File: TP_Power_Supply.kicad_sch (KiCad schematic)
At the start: 3 parts, among them U2 MCP1703T-3302E

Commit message: Issue 5 applied
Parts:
- U2: Developer (none) -> MW; LCSC Part #(optional) (none) -> C39051; Manufacturer (none) -> MICROCHIP TECHNOLOGY; Manufacturer Part Number (none) -> MCP1703T-3302E/CB; Package (none) -> SOT-23(SOT-23-3); Price@1000pcs (none) -> 1,49; Price@1pc (none) -> 2,04; Supplier (none) -> TME; Supplier Part Number (none) -> MCP1703T3302ECB; URL (none) -> https://www.tme.eu/pl/details/mcp1703t3302ecb/stabilizatory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
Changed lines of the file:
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@@
     (pin "2")
   )
-  (symbol (lib_id "Linear_Regulators:MCP1703T-3302E") (at 212.09 142.24 0) (unit 1)
+  (symbol (lib_name "Linear_Regulators:MCP1703T-3302E_1") (lib_id "Linear_Regulators:MCP1703T-3302E") (at 212.09 142.24 0) (unit 1)
     (in_bom yes) (on_board yes)
-    (property "Reference" "U2" (id 0) (at 212.09 132.4102 0)
+    (property "Reference" "U2" (id 0) (at 212.09 132.463 0)
       (effects (font (size 1.524 1.524)))
     )
-    (property "Value" "MCP1703T-3302E" (id 1) (at 212.09 135.1026 0)
+    (property "Value" "MCP1703T-3302E" (id 1) (at 212.09 135.1711 0)
       (effects (font (size 1.524 1.524)))
     )
@@
       (effects (font (size 1.524 1.524)) hide)
     )
-    (property "Datasheet" "Dc_Dc_Regulators/Linear/Components_Documentation/Mcp1703T_22049a.pdf" (id 3) (at 212.09 135.1026 0)
+    (property "Datasheet" "https://datasheet.lcsc.com/szlcsc/1808291012_Microchip-Tech-MCP1700T-3302E-TT_C39051.pdf" (id 3) (at 212.09 143.51 0)
       (effects (font (size 1.524 1.524)) hide)
     )
+    (property "Manufacturer" "MICROCHIP TECHNOLOGY" (id 4) (at 212.09 142.24 0)
+      (effects (font (size 1.27 1.27)) hide)
+    )
+    (property "Manufacturer Part Number" "MCP1703T-3302E/CB" (id 5) (at 212.09 142.24 0)
+      (effects (font (size 1.27 1.27)) hide)
+    )
+    (property "Supplier" "TME" (id 6) (at 212.09 142.24 0)
+      (effects (font (size 1.27 1.27)) hide)
+    )
+    (property "Supplier Part Number" "MCP1703T3302ECB" (id 7) (at 212.09 142.24 0)
+      (effects (font (size 1.27 1.27)) hide)
+    )
+    (property "URL" "https://www.tme.eu/pl/details/mcp1703t3302ecb/stabilizatory-napiecia-nieregulowane-ldo/microchip-technology/mcp1703t-3302e-cb/" (id 8) (at 212.09 142.24 0)
+      (effects (font (size 1.27 1.27)) hide)
+    )
+    (property "Price@1pc" "2,04" (id 9) (at 212.09 142.24 0)
+      (effects (font (size 1.27 1.27)) hide)
+    )
+    (property "Price@1000pcs" "1,49" (id 10) (at 212.09 142.24 0)
+      (effects (font (size 1.27 1.27)) hide)
+    )
+    (property "Developer" "MW" (id 11) (at 212.09 142.24 0)
+      (effects (font (size 1.27 1.27)) hide)
+    )
+    (property "Package" "SOT-23(SOT-23-3)" (id 12) (at 212.09 142.24 0)
+      (effects (font (size 1.27 1.27)) hide)
+    )
+    (property "LCSC Part #(optional)" "C39051" (id 13) (at 212.09 142.24 0)
+      (effects (font (size 1.27 1.27)) hide)
+    )
     (pin "1")

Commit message: Applied issue 4
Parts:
- removed C3, C4: 100nF/50V, Capacitors_Smd_0603:100nF_0603, symbol Capacitors_Smd0603:100nF_0603
- added C3, C4: 1uF/16V, Capacitors_Smd_0603:1uF_0603, symbol Capacitors_Smd0603:1uF
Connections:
- net GND: now also C3.2, C4.2
- net VIN: now also C3.1
- net VOUT_3.3V_250mA: now also C4.1
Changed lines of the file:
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@@
     (pin "1")
   )
-  (symbol (lib_id "Capacitors_Smd0603:100nF_0603") (at 191.77 147.32 0) (unit 1)
+  (symbol (lib_id "Capacitors_Smd0603:1uF") (at 191.77 147.32 0) (unit 1)
     (in_bom yes) (on_board yes)
-    (property "Reference" "C3" (id 0) (at 195.0974 146.1516 0)
+    (property "Reference" "C3" (id 0) (at 195.0975 146.1706 0)
       (effects (font (size 1.27 1.27)) (justify left))
     )
-    (property "Value" "100nF/50V" (id 1) (at 195.0974 148.463 0)
+    (property "Value" "1uF/16V" (id 1) (at 195.098 148.469 0)
       (effects (font (size 1.27 1.27)) (justify left))
     )
-    (property "Footprint" "Capacitors_Smd_0603:100nF_0603" (id 2) (at 191.77 147.32 0)
+    (property "Footprint" "Capacitors_Smd_0603:1uF_0603" (id 2) (at 187.96 142.24 0)
       (effects (font (size 1.524 1.524)) hide)
     )
-    (property "Datasheet" "Capacitors/Smd_0603/Components_Documentation/KEM_C1005_Y5V_SMD.pdf" (id 3) (at 191.77 147.32 0)
+    (property "Datasheet" "Capacitors/Smd_0603/Components_Documentation/KEM_C1005_Y5V_SMD.pdf" (id 3) (at 187.96 142.24 0)
       (effects (font (size 1.524 1.524)) hide)
     )
@@
       (effects (font (size 1.27 1.27)) hide)
     )
-    (property "Manufacturer Part Number" "CL10B104JB8NNNC" (id 5) (at 191.77 147.32 0)
+    (property "Manufacturer Part Number" "CL10B105KO8NNNC" (id 5) (at 191.77 147.32 0)
       (effects (font (size 1.27 1.27)) hide)
     )
@@
       (effects (font (size 1.27 1.27)) hide)
     )
-    (property "Supplier Part Number" "CL10B104JB8NNNC" (id 7) (at 191.77 147.32 0)
+    (property "Supplier Part Number" "CL10B105KO8NNNC" (id 7) (at 191.77 147.32 0)
       (effects (font (size 1.27 1.27)) hide)
     )
-    (property "URL" "https://www.tme.eu/pl/details/cl10b104jb8nnnc/kondensatory-mlcc-smd-0603/samsung/" (id 8) (at 191.77 147.32 0)
+    (property "URL" "https://www.tme.eu/pl/details/cl10b105ko8nnnc/kondensatory-mlcc-smd-0603/samsung/" (id 8) (at 191.77 147.32 0)
       (effects (font (size 1.27 1.27)) hide)
     )
-    (property "Price@1pc" "0,04540" (id 9) (at 191.77 147.32 0)
+    (property "Price@1pc" "0,07530" (id 9) (at 191.77 147.32 0)
       (effects (font (size 1.27 1.27)) hide)
     )
-    (property "Price@1000pcs" "0,02231" (id 10) (at 191.77 147.32 0)
+    (property "Price@1000pcs" "0,03514" (id 10) (at 191.77 147.32 0)
       (effects (font (size 1.27 1.27)) hide)
     )
@@
     (pin "2")
   )
-  (symbol (lib_id "Capacitors_Smd0603:100nF_0603") (at 232.41 147.32 0) (unit 1)
+  (symbol (lib_id "Capacitors_Smd0603:1uF") (at 232.41 147.32 0) (unit 1)
     (in_bom yes) (on_board yes)
-    (property "Reference" "C4" (id 0) (at 235.7374 146.1516 0)
+    (property "Reference" "C4" (id 0) (at 235.7375 146.1706 0)
       (effects (font (size 1.27 1.27)) (justify left))
     )
-    (property "Value" "100nF/50V" (id 1) (at 235.7374 148.463 0)
+    (property "Value" "1uF/16V" (id 1) (at 235.738 148.469 0)
       (effects (font (size 1.27 1.27)) (justify left))
     )
-    (property "Footprint" "Capacitors_Smd_0603:100nF_0603" (id 2) (at 232.41 147.32 0)
+    (property "Footprint" "Capacitors_Smd_0603:1uF_0603" (id 2) (at 228.6 142.24 0)
       (effects (font (size 1.524 1.524)) hide)
     )
-    (property "Datasheet" "Capacitors/Smd_0603/Components_Documentation/KEM_C1005_Y5V_SMD.pdf" (id 3) (at 232.41 147.32 0)
+    (property "Datasheet" "Capacitors/Smd_0603/Components_Documentation/KEM_C1005_Y5V_SMD.pdf" (id 3) (at 228.6 142.24 0)
       (effects (font (size 1.524 1.524)) hide)
     )
@@
       (effects (font (size 1.27 1.27)) hide)
     )
-    (property "Manufacturer Part Number" "CL10B104JB8NNNC" (id 5) (at 232.41 147.32 0)
+    (property "Manufacturer Part Number" "CL10B105KO8NNNC" (id 5) (at 232.41 147.32 0)
       (effects (font (size 1.27 1.27)) hide)
     )
@@
       (effects (font (size 1.27 1.27)) hide)
     )
-    (property "Supplier Part Number" "CL10B104JB8NNNC" (id 7) (at 232.41 147.32 0)
+    (property "Supplier Part Number" "CL10B105KO8NNNC" (id 7) (at 232.41 147.32 0)
       (effects (font (size 1.27 1.27)) hide)
     )
-    (property "URL" "https://www.tme.eu/pl/details/cl10b104jb8nnnc/kondensatory-mlcc-smd-0603/samsung/" (id 8) (at 232.41 147.32 0)
+    (property "URL" "https://www.tme.eu/pl/details/cl10b105ko8nnnc/kondensatory-mlcc-smd-0603/samsung/" (id 8) (at 232.41 147.32 0)
       (effects (font (size 1.27 1.27)) hide)
     )
-    (property "Price@1pc" "0,04540" (id 9) (at 232.41 147.32 0)
+    (property "Price@1pc" "0,07530" (id 9) (at 232.41 147.32 0)
       (effects (font (size 1.27 1.27)) hide)
     )
-    (property "Price@1000pcs" "0,02231" (id 10) (at 232.41 147.32 0)
+    (property "Price@1000pcs" "0,03514" (id 10) (at 232.41 147.32 0)
       (effects (font (size 1.27 1.27)) hide)
     )

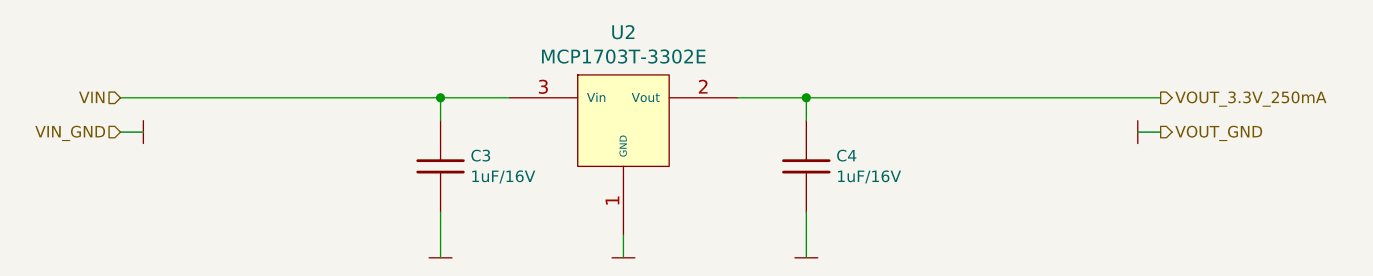
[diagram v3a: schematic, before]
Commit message: Reworked schematic and applied changes on pcb related with mini pci express
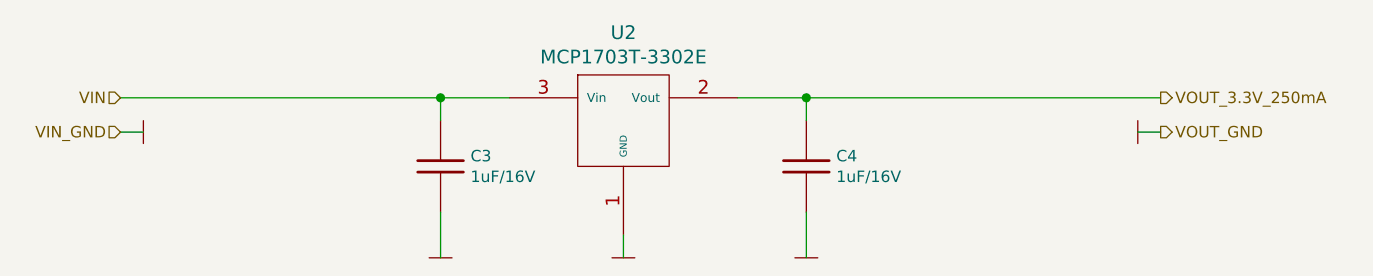
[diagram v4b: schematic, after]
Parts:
- removed C3, C4: 1uF/16V, Capacitors_Smd_0603:1uF_0603, symbol Capacitors_Smd0603:1uF
- added C3, C4: 1uF/16V, Capacitors_Smd_0603:1uF_0603, symbol Capacitors_Smd0603:1uF_0603
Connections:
- net GND: now also C3.2, C4.2
- net VIN: now also C3.1
- net VOUT_3.3V_250mA: now also C4.1
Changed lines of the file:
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@@
     (pin "1")
   )
-  (symbol (lib_id "Capacitors_Smd0603:1uF") (at 191.77 147.32 0) (unit 1)
+  (symbol (lib_id "Capacitors_Smd0603:1uF_0603") (at 191.77 147.32 0) (unit 1)
     (in_bom yes) (on_board yes)
-    (property "Reference" "C3" (id 0) (at 195.0975 146.1706 0)
+    (property "Reference" "C3" (id 0) (at 195.098 146.171 0)
       (effects (font (size 1.27 1.27)) (justify left))
     )
@@
     (pin "2")
   )
-  (symbol (lib_id "Capacitors_Smd0603:1uF") (at 232.41 147.32 0) (unit 1)
+  (symbol (lib_id "Capacitors_Smd0603:1uF_0603") (at 232.41 147.32 0) (unit 1)
     (in_bom yes) (on_board yes)
-    (property "Reference" "C4" (id 0) (at 235.7375 146.1706 0)
+    (property "Reference" "C4" (id 0) (at 235.738 146.171 0)
       (effects (font (size 1.27 1.27)) (justify left))
     )
@@
     (pin "2")
   )
-  (symbol (lib_name "Linear_Regulators:MCP1703T-3302E_1") (lib_id "Linear_Regulators:MCP1703T-3302E") (at 212.09 142.24 0) (unit 1)
+  (symbol (lib_id "Linear_Regulators:MCP1703T-3302E") (at 212.09 142.24 0) (unit 1)
     (in_bom yes) (on_board yes)
     (property "Reference" "U2" (id 0) (at 212.09 132.463 0)
@@
       (effects (font (size 1.524 1.524)) hide)
     )
-    (property "Datasheet" "https://datasheet.lcsc.com/szlcsc/1808291012_Microchip-Tech-MCP1700T-3302E-TT_C39051.pdf" (id 3) (at 212.09 143.51 0)
+    (property "Datasheet" "Dc_Dc_Regulators/Linear/Components_Documentation/Mcp1703T_22049a.pdf" (id 3) (at 212.09 143.51 0)
       (effects (font (size 1.524 1.524)) hide)
     )
